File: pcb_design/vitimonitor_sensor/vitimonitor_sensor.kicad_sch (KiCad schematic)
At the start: 45 parts, among them J1 USB_C_Receptacle_USB2.0_14P, J2 Conn_01x10, J3 Conn_01x02, J4 Conn_01x04, J5 Pin_2x5, J6 Conn_01x04, Q2 Si2371EDS, SW1 BOOT, SW2 RESETN, U1 ESP32-C3-WROOM-02U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

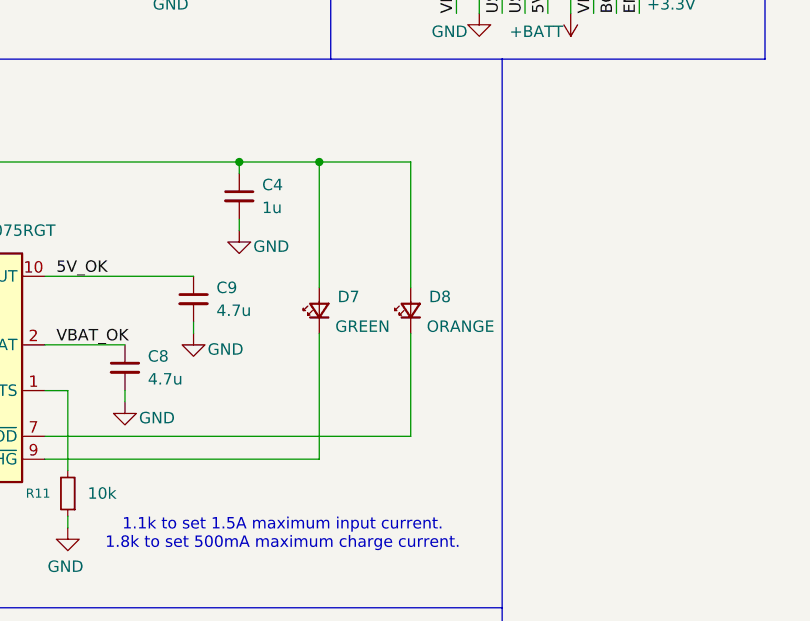
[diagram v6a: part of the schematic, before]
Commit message: Resistor in series to charger leds
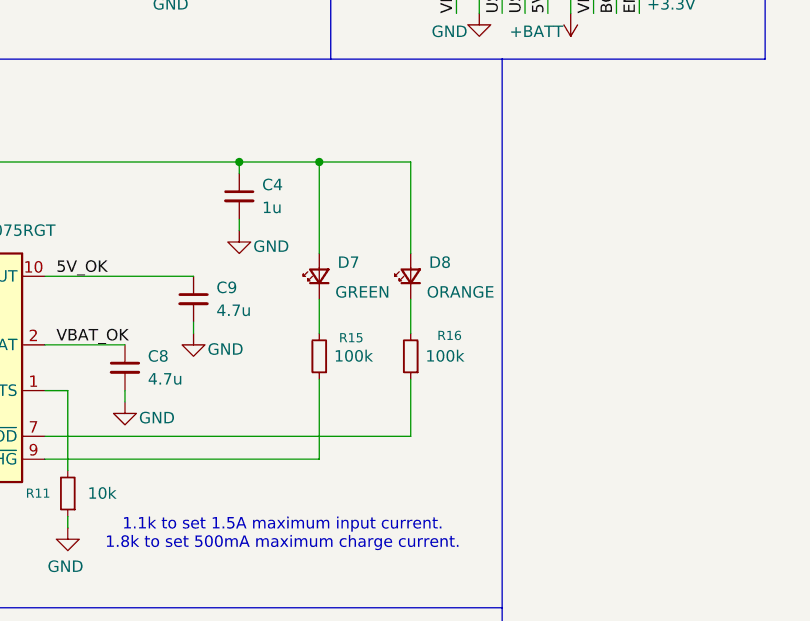
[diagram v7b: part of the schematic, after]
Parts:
- added R15, R16: 100k, symbol Device:R_Small
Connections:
- net at U5.7 (~{PGOOD}): now also R16.1; no longer D8.1 (K)
- net at U5.9 (~{CHG}): now also R15.1; no longer D7.1 (K)
- new net: D8.1 (K), R16.2
- new net: D7.1 (K), R15.2
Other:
- moved on the sheet: D7, D8
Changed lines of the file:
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@@
 	(wire
 		(pts
+			(xy 100.33 111.76) (xy 100.33 118.11)
+		)
+		(stroke
+			(width 0)
+			(type default)
+		)
+	)
+	(wire
+		(pts
 			(xy 16.51 100.33) (xy 34.29 100.33)
 		)
@@
 	(wire
 		(pts
+			(xy 100.33 102.87) (xy 100.33 106.68)
+		)
+		(stroke
+			(width 0)
+			(type default)
+		)
+	)
+	(wire
+		(pts
 			(xy 102.87 158.75) (xy 107.95 158.75)
 		)
@@
 	(wire
 		(pts
-			(xy 100.33 106.68) (xy 100.33 118.11)
-		)
-		(stroke
-			(width 0)
-			(type default)
-		)
-	)
-	(wire
-		(pts
 			(xy 50.8 50.8) (xy 53.34 50.8)
 		)
@@
 	(wire
 		(pts
-			(xy 90.17 87.63) (xy 90.17 101.6)
+			(xy 90.17 87.63) (xy 90.17 97.79)
 		)
 		(stroke
@@
 	(wire
 		(pts
-			(xy 100.33 87.63) (xy 100.33 101.6)
+			(xy 100.33 87.63) (xy 100.33 97.79)
 		)
 		(stroke
@@
 	(wire
 		(pts
-			(xy 90.17 106.68) (xy 90.17 120.65)
-		)
-		(stroke
-			(width 0)
-			(type default)
-		)
-	)
-	(wire
-		(pts
 			(xy 64.77 181.61) (xy 68.58 181.61)
 		)
@@
 	(wire
 		(pts
+			(xy 90.17 111.76) (xy 90.17 120.65)
+		)
+		(stroke
+			(width 0)
+			(type default)
+		)
+	)
+	(wire
+		(pts
 			(xy 21.59 158.75) (xy 40.64 158.75)
 		)
@@
 		)
 	)
+	(wire
+		(pts
+			(xy 90.17 102.87) (xy 90.17 106.68)
+		)
+		(stroke
+			(width 0)
+			(type default)
+		)
+	)
 	(label "UART_RX"
 		(at 52.07 156.21 0)
@@
 	(symbol
 		(lib_id "Device:LED_Small")
-		(at 100.33 104.14 90)
+		(at 100.33 100.33 90)
 		(unit 1)
 		(exclude_from_sim no)
@@
 		(dnp no)
 		(property "Reference" "D8"
-			(at 102.362 102.616 90)
+			(at 102.362 98.806 90)
 			(effects
 				(font
@@
 		)
 		(property "Value" "ORANGE"
-			(at 102.108 105.918 90)
+			(at 102.108 102.108 90)
 			(effects
 				(font
@@
 		)
 		(property "Footprint" ""
-			(at 100.33 104.14 90)
+			(at 100.33 100.33 90)
 			(effects
 				(font
@@
 		)
 		(property "Datasheet" "~"
-			(at 100.33 104.14 90)
+			(at 100.33 100.33 90)
 			(effects
 				(font
@@
 		)
 		(property "Description" "Light emitting diode, small symbol"
-			(at 100.33 104.14 0)
+			(at 100.33 100.33 0)
 			(effects
 				(font
@@
 		)
 		(property "Sim.Pin" "1=K 2=A"
-			(at 100.33 104.14 0)
+			(at 100.33 100.33 0)
 			(effects
 				(font
@@
 	(symbol
 		(lib_id "Device:LED_Small")
-		(at 90.17 104.14 90)
+		(at 90.17 100.33 90)
 		(unit 1)
 		(exclude_from_sim no)
@@
 		(dnp no)
 		(property "Reference" "D7"
-			(at 92.202 102.616 90)
+			(at 92.202 98.806 90)
 			(effects
 				(font
@@
 		)
 		(property "Value" "GREEN"
-			(at 91.948 105.918 90)
+			(at 91.948 102.108 90)
 			(effects
 				(font
@@
 		)
 		(property "Footprint" ""
-			(at 90.17 104.14 90)
+			(at 90.17 100.33 90)
 			(effects
 				(font
@@
 		)
 		(property "Datasheet" "~"
-			(at 90.17 104.14 90)
+			(at 90.17 100.33 90)
 			(effects
 				(font
@@
 		)
 		(property "Description" "Light emitting diode, small symbol"
-			(at 90.17 104.14 0)
+			(at 90.17 100.33 0)
 			(effects
 				(font
@@
 		)
 		(property "Sim.Pin" "1=K 2=A"
-			(at 90.17 104.14 0)
+			(at 90.17 100.33 0)
 			(effects
 				(font
@@
 	)
 	(symbol
+		(lib_id "Device:R_Small")
+		(at 100.33 109.22 180)
+		(unit 1)
+		(exclude_from_sim no)
+		(in_bom yes)
+		(on_board yes)
+		(dnp no)
+		(property "Reference" "R16"
+			(at 104.648 106.934 0)
+			(effects
+				(font
+					(size 1.016 1.016)
+				)
+			)
+		)
+		(property "Value" "100k"
+			(at 104.14 109.22 0)
+			(effects
+				(font
+					(size 1.27 1.27)
+				)
+			)
+		)
+		(property "Footprint" ""
+			(at 100.33 109.22 0)
+			(effects
+				(font
+					(size 1.27 1.27)
+				)
+				(hide yes)
+			)
+		)
+		(property "Datasheet" "~"
+			(at 100.33 109.22 0)
+			(effects
+				(font
+					(size 1.27 1.27)
+				)
+				(hide yes)
+			)
+		)
+		(property "Description" "Resistor, small symbol"
+			(at 100.33 109.22 0)
+			(effects
+				(font
+					(size 1.27 1.27)
+				)
+				(hide yes)
+			)
+		)
+		(pin "2"
+		)
+		(pin "1"
+		)
+		(instances
+			(project "vitimonitor_sensor"
+				(path "/8365193e-4878-4a04-b89a-a51695e2c71c"
+					(reference "R16")
+					(unit 1)
+				)
+			)
+		)
+	)
+	(symbol
 		(lib_id "Diode:ESD9B3.3ST5G")
 		(at 68.58 186.69 90)
@@
 					(unit 1)
 				)
+			)
+		)
+	)
+	(symbol
+		(lib_id "Device:R_Small")
+		(at 90.17 109.22 180)
+		(unit 1)
+		(exclude_from_sim no)
+		(in_bom yes)
+		(on_board yes)
+		(dnp no)
+		(property "Reference" "R15"
+			(at 93.726 107.188 0)
+			(effects
+				(font
+					(size 1.016 1.016)
+				)
+			)
+		)
+		(property "Value" "100k"
+			(at 93.98 109.22 0)
+			(effects
+				(font
+					(size 1.27 1.27)
+				)
+			)
+		)
+		(property "Footprint" ""
+			(at 90.17 109.22 0)
+			(effects
+				(font
+					(size 1.27 1.27)
+				)
+				(hide yes)
+			)
+		)
+		(property "Datasheet" "~"
+			(at 90.17 109.22 0)
+			(effects
+				(font
+					(size 1.27 1.27)
+				)
+				(hide yes)
+			)
+		)
+		(property "Description" "Resistor, small symbol"
+			(at 90.17 109.22 0)
+			(effects
+				(font
+					(size 1.27 1.27)
+				)
+				(hide yes)
+			)
+		)
+		(pin "2"
+		)
+		(pin "1"
+		)
+		(instances
+			(project "vitimonitor_sensor"
+				(path "/8365193e-4878-4a04-b89a-a51695e2c71c"
+					(reference "R15")
+					(unit 1)
+				)

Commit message: Minor change
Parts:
- R15, R16: value 100k -> 10k
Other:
- moved on the sheet: D2, R3
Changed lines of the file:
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@@
 	(polyline
 		(pts
-			(xy 110.49 76.2) (xy 110.49 168.91)
-		)
-		(stroke
-			(width 0)
-			(type default)
-		)
-	)
-	(polyline
-		(pts
 			(xy 214.63 85.09) (xy 285.75 85.09)
 		)
@@
 	(polyline
 		(pts
-			(xy 110.49 168.91) (xy 110.49 196.85)
-		)
-		(stroke
-			(width 0)
-			(type default)
-		)
-	)
-	(polyline
-		(pts
-			(xy 12.7 168.91) (xy 110.49 168.91)
+			(xy 12.7 168.91) (xy 176.53 168.91)
 		)
 		(stroke
@@
 	(wire
 		(pts
-			(xy 204.47 27.94) (xy 204.47 29.21)
+			(xy 205.74 27.94) (xy 205.74 29.21)
 		)
 		(stroke
@@
 	(wire
 		(pts
-			(xy 204.47 21.59) (xy 204.47 22.86)
+			(xy 205.74 21.59) (xy 205.74 22.86)
 		)
 		(stroke
@@
 	(wire
 		(pts
-			(xy 204.47 34.29) (xy 204.47 35.56)
+			(xy 205.74 34.29) (xy 205.74 35.56)
 		)
 		(stroke
@@
 	(polyline
 		(pts
-			(xy 199.39 12.7) (xy 199.39 41.91)
+			(xy 200.66 12.7) (xy 200.66 41.91)
 		)
 		(stroke
@@
 		)
 	)
+	(polyline
+		(pts
+			(xy 110.49 76.2) (xy 110.49 168.91)
+		)
+		(stroke
+			(width 0)
+			(type default)
+		)
+	)
 	(wire
 		(pts
@@
 	(symbol
 		(lib_id "Device:LED_Small")
-		(at 204.47 31.75 90)
+		(at 205.74 31.75 90)
 		(unit 1)
 		(exclude_from_sim no)
@@
 		(dnp no)
 		(property "Reference" "D2"
-			(at 206.502 30.226 90)
+			(at 207.772 30.226 90)
 			(effects
 				(font
@@
 		)
 		(property "Value" "GREEN"
-			(at 206.248 33.528 90)
+			(at 207.01 33.782 90)
 			(effects
 				(font
@@
 		)
 		(property "Footprint" ""
-			(at 204.47 31.75 90)
+			(at 205.74 31.75 90)
 			(effects
 				(font
@@
 		)
 		(property "Datasheet" "~"
-			(at 204.47 31.75 90)
+			(at 205.74 31.75 90)
 			(effects
 				(font
@@
 		)
 		(property "Description" "Light emitting diode, small symbol"
-			(at 204.47 31.75 0)
+			(at 205.74 31.75 0)
 			(effects
 				(font
@@
 		)
 		(property "Sim.Pin" "1=K 2=A"
-			(at 204.47 31.75 0)
+			(at 205.74 31.75 0)
 			(effects
 				(font
@@
 	(symbol
 		(lib_id "power:GND")
-		(at 204.47 35.56 0)
+		(at 205.74 35.56 0)
 		(unit 1)
 		(exclude_from_sim no)
@@
 		(dnp no)
 		(property "Reference" "#PWR013"
-			(at 204.47 41.91 0)
+			(at 205.74 41.91 0)
 			(effects
 				(font
@@
 		)
 		(property "Value" "GND"
-			(at 204.47 39.624 0)
+			(at 205.74 39.624 0)
 			(effects
 				(font
@@
 		)
 		(property "Footprint" ""
-			(at 204.47 35.56 0)
+			(at 205.74 35.56 0)
 			(effects
 				(font
@@
 		)
 		(property "Datasheet" ""
-			(at 204.47 35.56 0)
+			(at 205.74 35.56 0)
 			(effects
 				(font
@@
 		)
 		(property "Description" "Power symbol creates a global label with name \"GND\" , ground"
-			(at 204.47 35.56 0)
+			(at 205.74 35.56 0)
 			(effects
 				(font
@@
 	(symbol
 		(lib_id "power:+3.3V")
-		(at 204.47 21.59 0)
+		(at 205.74 21.59 0)
 		(unit 1)
 		(exclude_from_sim no)
@@
 		(dnp no)
 		(property "Reference" "#PWR012"
-			(at 204.47 25.4 0)
+			(at 205.74 25.4 0)
 			(effects
 				(font
@@
 		)
 		(property "Value" "+3.3V"
-			(at 204.47 17.526 0)
+			(at 205.74 17.526 0)
 			(effects
 				(font
@@
 		)
 		(property "Footprint" ""
-			(at 204.47 21.59 0)
+			(at 205.74 21.59 0)
 			(effects
 				(font
@@
 		)
 		(property "Datasheet" ""
-			(at 204.47 21.59 0)
+			(at 205.74 21.59 0)
 			(effects
 				(font
@@
 		)
 		(property "Description" "Power symbol creates a global label with name \"+3.3V\""
-			(at 204.47 21.59 0)
+			(at 205.74 21.59 0)
 			(effects
 				(font
@@
 			)
 		)
-		(property "Value" "100k"
+		(property "Value" "10k"
 			(at 104.14 109.22 0)
 			(effects
@@
 	(symbol
 		(lib_id "Device:R_Small")
-		(at 204.47 25.4 0)
+		(at 205.74 25.4 0)
 		(unit 1)
 		(exclude_from_sim no)
@@
 		(dnp no)
 		(property "Reference" "R3"
-			(at 207.518 23.876 0)
+			(at 208.788 23.876 0)
 			(effects
 				(font
@@
 		)
 		(property "Value" "1k"
-			(at 208.026 27.432 0)
+			(at 209.296 27.432 0)
 			(effects
 				(font
@@
 		)
 		(property "Footprint" ""
-			(at 204.47 25.4 0)
+			(at 205.74 25.4 0)
 			(effects
 				(font
@@
 		)
 		(property "Datasheet" "~"
-			(at 204.47 25.4 0)
+			(at 205.74 25.4 0)
 			(effects
 				(font
@@
 		)
 		(property "Description" "Resistor, small symbol"
-			(at 204.47 25.4 0)
+			(at 205.74 25.4 0)
 			(effects
 				(font
@@
 			)
 		)
-		(property "Value" "100k"
+		(property "Value" "10k"
 			(at 93.98 109.22 0)
 			(effects
